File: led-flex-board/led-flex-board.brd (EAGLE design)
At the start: 20 x 15 mm, 30 parts

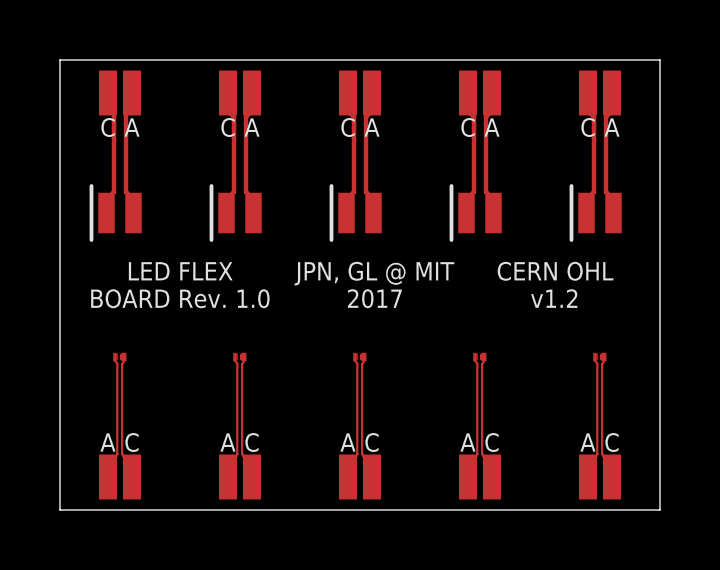
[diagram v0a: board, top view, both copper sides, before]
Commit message: Added more designs to led-flex-board
- Multiple lead length options
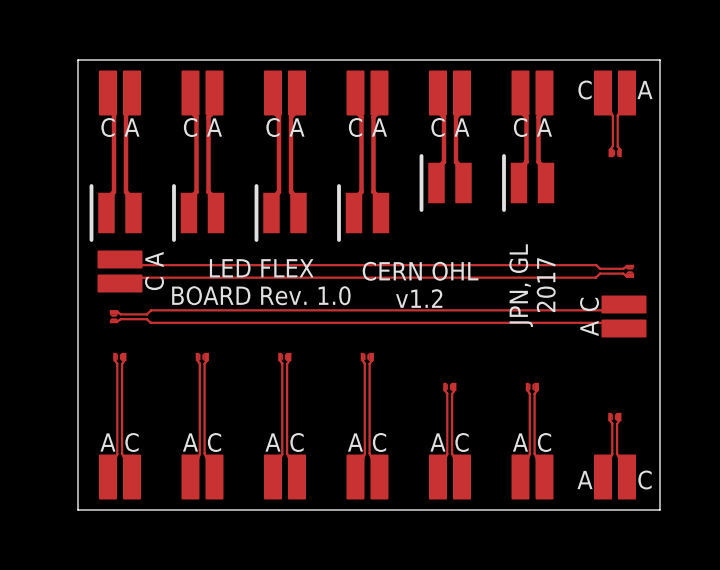
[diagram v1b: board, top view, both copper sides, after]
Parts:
- added A10, A11, A12, A13, A15, A16, C10, C11, C12, C13, C15, C16: (no value), jonnew:S0.6X1.5MM
- added D11, D12, D14, D16, D17: DA2432, jonnew:DA2432
- added D13: XQ-E, jonnew:XLAMP_1.6X1.6MM
- D1: value (none) -> DA2432
- D10, D6, D7, D8, D9: value DA2432 -> XQ-E
- moved D5 5.10 mm to (12.0, 4.10)
- moved D6 5.10 mm to (12.0, 10.9)
- moved A4 5.00 mm to (11.6, 1.10)
- moved C5 5.00 mm to (11.6, 13.9)
- moved A5 5.00 mm to (12.4, 13.9)
- moved C4 5.00 mm to (12.4, 1.10)
- moved A3 3.75 mm to (8.85, 1.10)
- moved A6 3.75 mm to (9.65, 13.9)
- moved C3 3.75 mm to (9.65, 1.10)
- moved C6 3.75 mm to (8.85, 13.9)
- moved D4 3.75 mm to (9.25, 5.10)
- moved D7 3.75 mm to (9.25, 9.90)
- moved A2 2.50 mm to (6.10, 1.10)
- moved A7 2.50 mm to (6.90, 13.9)
- moved C2 2.50 mm to (6.90, 1.10)
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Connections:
- new net N$21: C10.TP, D11.C
- new net N$22: A10.TP, D11.A
- new net N$23: C11.TP, D12.C
- new net N$24: A11.TP, D12.A
- new net N$25: C12.TP, D13.C
- new net N$26: A12.TP, D13.A
- new net N$27: C13.TP, D14.C
- new net N$28: A13.TP, D14.A
- new net N$31: C15.TP, D16.C
- new net N$32: A15.TP, D16.A
- new net N$33: C16.TP, D17.C
- new net N$34: A16.TP, D17.A
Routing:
- net N$33: track 0.00 -> 17.1 mm
- net N$31: track 0.00 -> 17.1 mm
- net N$34: track 0.00 -> 17.1 mm
- net N$32: track 0.00 -> 17.1 mm
- net N$26: track 0.00 -> 3.19 mm
- net N$25: track 0.00 -> 3.19 mm
- net N$21: track 0.00 -> 3.09 mm
- net N$22: track 0.00 -> 3.09 mm
- net N$27: track 0.00 -> 2.09 mm
- net N$23: track 0.00 -> 2.09 mm
- net N$28: track 0.00 -> 2.09 mm
- net N$24: track 0.00 -> 2.09 mm
- net N$9: track 4.09 -> 3.09 mm
- net N$10: track 4.09 -> 3.09 mm
- net N$12: track 4.19 -> 3.19 mm
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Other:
- board size 20 x 15 mm -> 19.4 x 15 mm
- board text added: "JPN, GL 2017"
- board text removed: "JPN, GL @ MIT 2017"
